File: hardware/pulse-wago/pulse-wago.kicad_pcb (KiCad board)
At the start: 4 copper layers, 180 x 40 mm, 170 parts, among them J1001 WAGO 2601-1101, J1002 WAGO 2601-1101, J101 Cortex, J1101 WAGO 2601-1101, J1102 WAGO 2601-1101, J1201 WAGO 2601-1101, J1202 WAGO 2601-1101, J1301 WAGO 2601-1101, J1302 WAGO 2601-1101, J1401 WAGO 2601-1101, J1402 WAGO 2601-1101, J1501 WAGO 2601-1101, J1502 WAGO 2601-1101, J1601 WAGO 2601-1101, J1602 WAGO 2601-1101, J1701 WAGO 2601-1101, J1702 WAGO 2601-1101, J1801 WAGO 2065-100, J1802 WAGO 2065-100, J1901 2x05_Horizontal, J2001 2x05_Horizontal, J201 WAGO 2601-1101, J202 WAGO 2601-1101, J301 WAGO 2601-1101, J302 WAGO 2601-1101, J401 WAGO 2601-1101, J402 WAGO 2601-1101, J501 WAGO 2601-1101, J502 WAGO 2601-1101, J601 WAGO 2601-1101, J602 WAGO 2601-1101, J701 WAGO 2601-1101, J702 WAGO 2601-1101, J801 WAGO 2601-1101, J802 WAGO 2601-1101, J901 WAGO 2601-1101, J902 WAGO 2601-1101, Q1001 BSC010N04LS, Q1101 BSC010N04LS, Q1201 BSC010N04LS, Q1301 BSC010N04LS, Q1401 BSC010N04LS, Q1501 BSC010N04LS, Q1601 BSC010N04LS, Q1701 BSC010N04LS, Q201 BSC010N04LS, Q301 BSC010N04LS, Q401 BSC010N04LS, Q501 BSC010N04LS, Q601 BSC010N04LS, Q701 BSC010N04LS, Q801 BSC010N04LS, Q901 BSC010N04LS, SW101 SKSG, SW102 SKSG, U101 TPS78433QWDRBRQ1, U102 ATSAMD51J, U1801 BTT6010, Y101 32k768

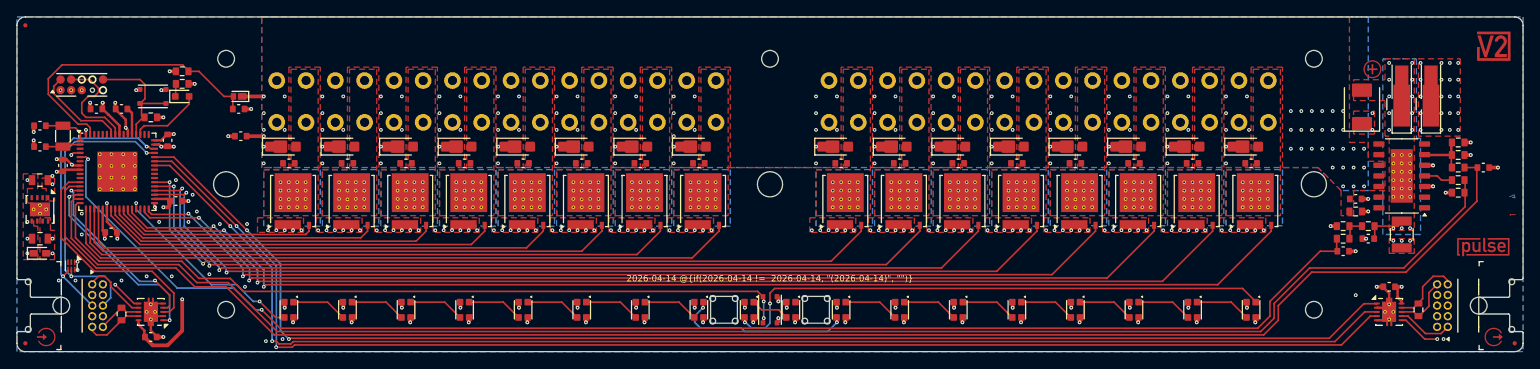
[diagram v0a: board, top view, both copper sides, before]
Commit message: Switch to 6 layer
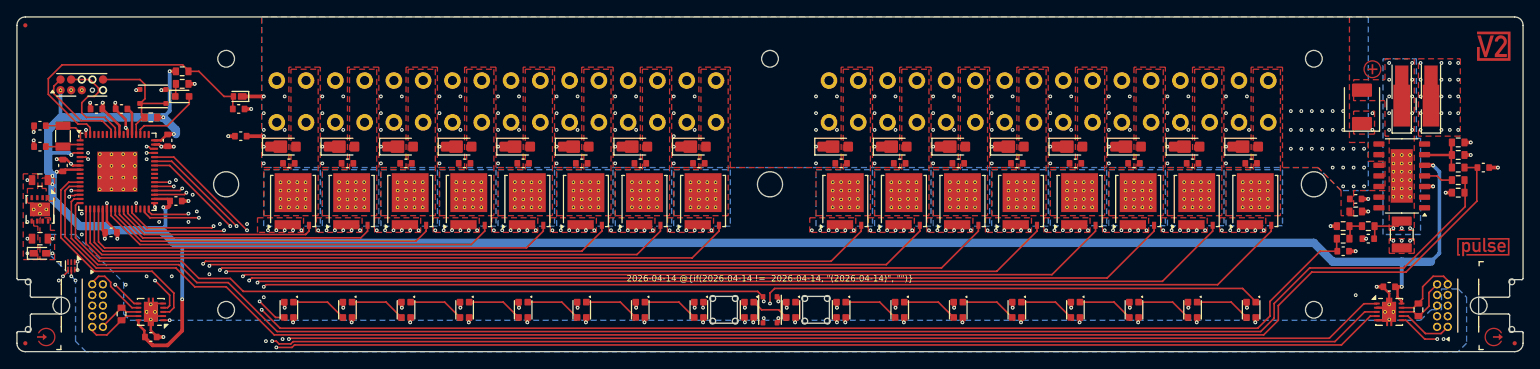
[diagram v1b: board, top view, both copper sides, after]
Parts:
- C1001, C101, C102, C104, C106, C107, C108, C109, C110, C1101, C1201, C1301, C1401, C1501, C1601, C1701, C1801, C1803, C1804, C1805, C1806, C1807, C1901, C2001, C201, C301, C401, C501, C601, C701, C801, C901: footprint V2_Capacitor_SMD:C_0603 -> V2_Capacitor_SMD:C_1608
- C103, C105: footprint V2_Capacitor_SMD:C_0805 -> V2_Capacitor_SMD:C_2012
- C1802: footprint V2_Capacitor_SMD:C_1210 -> V2_Capacitor_SMD:C_3225
- D102: footprint V2_LED:LED_0603 -> V2_LED:LED_1608
- INFO101: value Layer_Numbers -> Layer_Numbers-6; footprint V2_Production:Layer_Numbers -> V2_Production:Layer_Numbers-6
- R101, R102, R1801, R1802, R1803, R1804, R1805, R1806, R1807, R1808, R1809, R1810, R1901, R2001: footprint V2_Resistor_SMD:R_0603 -> V2_Resistor_SMD:R_1608
- TVS101: footprint V2_Diode_SMD:D_0603 -> V2_Diode_SMD:D_1608
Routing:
- net +3V3: track 35.7 -> 269.3 mm
- net /USB-: track 35.9 -> 37.2 mm
- net GND: vias 196 -> 198
- added copper zone on B.Cu, net +5V
- added copper zone on In3.Cu, net GND
- added copper zone on In4.Cu, net GND
- removed copper zone on In2.Cu, net +3V3
- removed copper zone on In2.Cu, net +5V
- removed copper zone on In1.Cu, net /PWM Channel 1/PWM-Sink
- removed copper zone on In2.Cu, net /PWM Channel 1/PWM-Sink
- removed copper zone on In1.Cu, net /PWM Channel 10/PWM-Sink
- removed copper zone on In2.Cu, net /PWM Channel 10/PWM-Sink
- removed copper zone on In1.Cu, net /PWM Channel 11/PWM-Sink
- removed copper zone on In2.Cu, net /PWM Channel 11/PWM-Sink
- removed copper zone on In1.Cu, net /PWM Channel 12/PWM-Sink
- removed copper zone on In2.Cu, net /PWM Channel 12/PWM-Sink
- removed copper zone on In1.Cu, net /PWM Channel 13/PWM-Sink
- removed copper zone on In2.Cu, net /PWM Channel 13/PWM-Sink
- removed copper zone on In1.Cu, net /PWM Channel 14/PWM-Sink
- removed copper zone on In2.Cu, net /PWM Channel 14/PWM-Sink
- removed copper zone on In1.Cu, net /PWM Channel 15/PWM-Sink
- removed copper zone on In2.Cu, net /PWM Channel 15/PWM-Sink
- removed copper zone on In1.Cu, net /PWM Channel 16/PWM-Sink
- removed copper zone on In2.Cu, net /PWM Channel 16/PWM-Sink
- removed copper zone on In1.Cu, net /PWM Channel 2/PWM-Sink
- removed copper zone on In2.Cu, net /PWM Channel 2/PWM-Sink
- removed copper zone on In1.Cu, net /PWM Channel 3/PWM-Sink
- removed copper zone on In2.Cu, net /PWM Channel 3/PWM-Sink
- removed copper zone on In1.Cu, net /PWM Channel 4/PWM-Sink
- removed copper zone on In2.Cu, net /PWM Channel 4/PWM-Sink
- removed copper zone on In1.Cu, net /PWM Channel 5/PWM-Sink
- removed copper zone on In2.Cu, net /PWM Channel 5/PWM-Sink
- removed copper zone on In1.Cu, net /PWM Channel 6/PWM-Sink
- removed copper zone on In2.Cu, net /PWM Channel 6/PWM-Sink
- removed copper zone on In1.Cu, net /PWM Channel 7/PWM-Sink
- removed copper zone on In2.Cu, net /PWM Channel 7/PWM-Sink
- removed copper zone on In1.Cu, net /PWM Channel 8/PWM-Sink
- removed copper zone on In2.Cu, net /PWM Channel 8/PWM-Sink
- removed copper zone on In1.Cu, net /PWM Channel 9/PWM-Sink
- removed copper zone on In2.Cu, net /PWM Channel 9/PWM-Sink
- removed copper zone on In1.Cu, net /Power +28V/+28V-Supply
- removed copper zone on In2.Cu, net /Power +28V/+28V-Supply
- removed copper zone on B.Cu, net GND
- removed copper zone on In2.Cu, net GND
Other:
- copper layers 4 -> 6

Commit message: Update
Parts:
- moved ICON101 0.25 mm to (243.2, 78.5)
- renumbered C1301 to C1101, C1101 to C1301, C1701 to C1501, C1501 to C1701, D1301 to D1101, D1302 to D1102, D1101 to D1301, D1102 to D1302, D1701 to D1501, D1702 to D1502, D1501 to D1701, D1502 to D1702, J1301 to J1101, J1302 to J1102, J1101 to J1301, J1102 to J1302, J1701 to J1501, J1702 to J1502, J1501 to J1701, J1502 to J1702, Q1301 to Q1101, Q1101 to Q1301, Q1701 to Q1501, Q1501 to Q1701
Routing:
- net /Link Socket/TX-Y: track 6.68 -> 4.58 mm
- net GND: vias 198 -> 231
